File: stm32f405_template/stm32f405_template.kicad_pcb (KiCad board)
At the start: 2 copper layers, 51 x 71 mm, 55 parts, among them J1 USB_B, J2 Conn_01x08, J3 Conn_01x08, J4 Conn_01x02, J5 Conn_01x08, J6 Conn_01x08, J7 Conn_01x02, J8 Conn_01x02, Q1 2N3904, Q2 2N3904, SW1 SW_RESET, U1 STM32F405RGTx, U2 MCP1700-3302E_TO92, Y1 14MHz, Y2 32.768 kHz

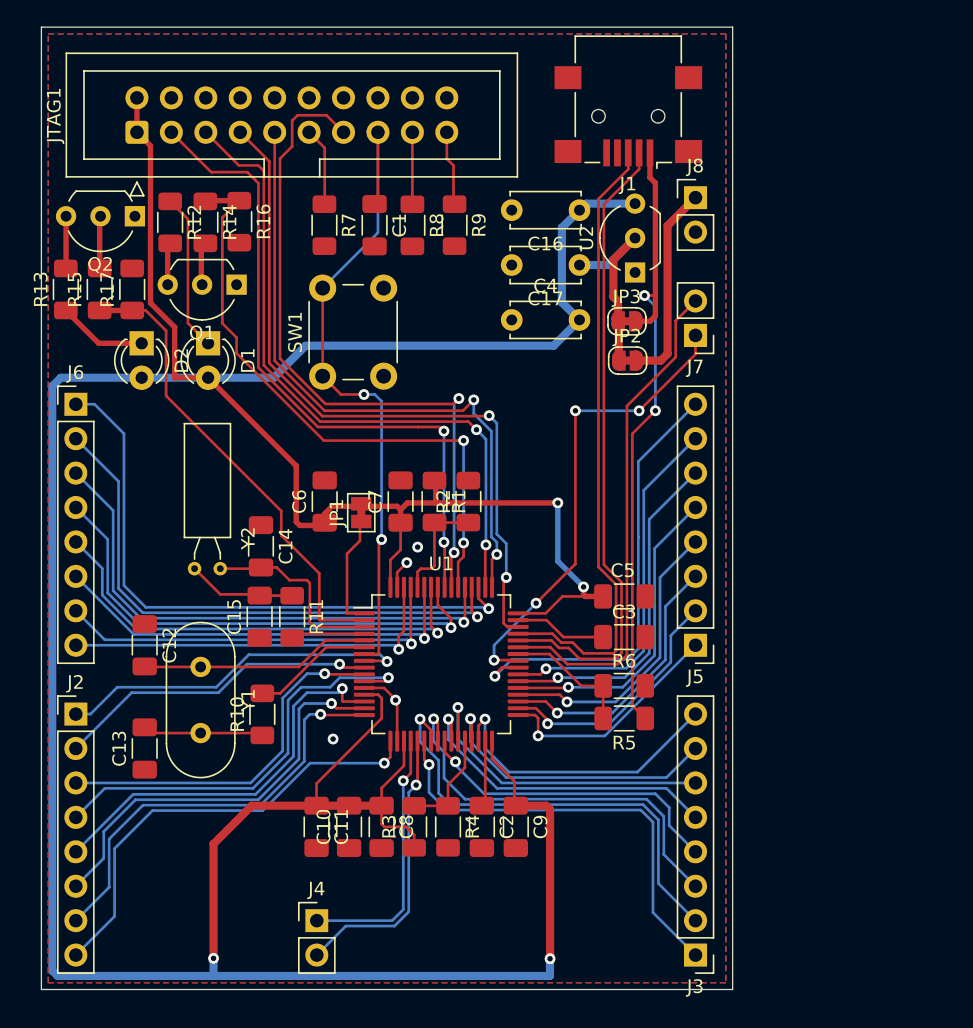
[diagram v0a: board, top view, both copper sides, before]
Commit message: Geographic re-annotate and cleanup
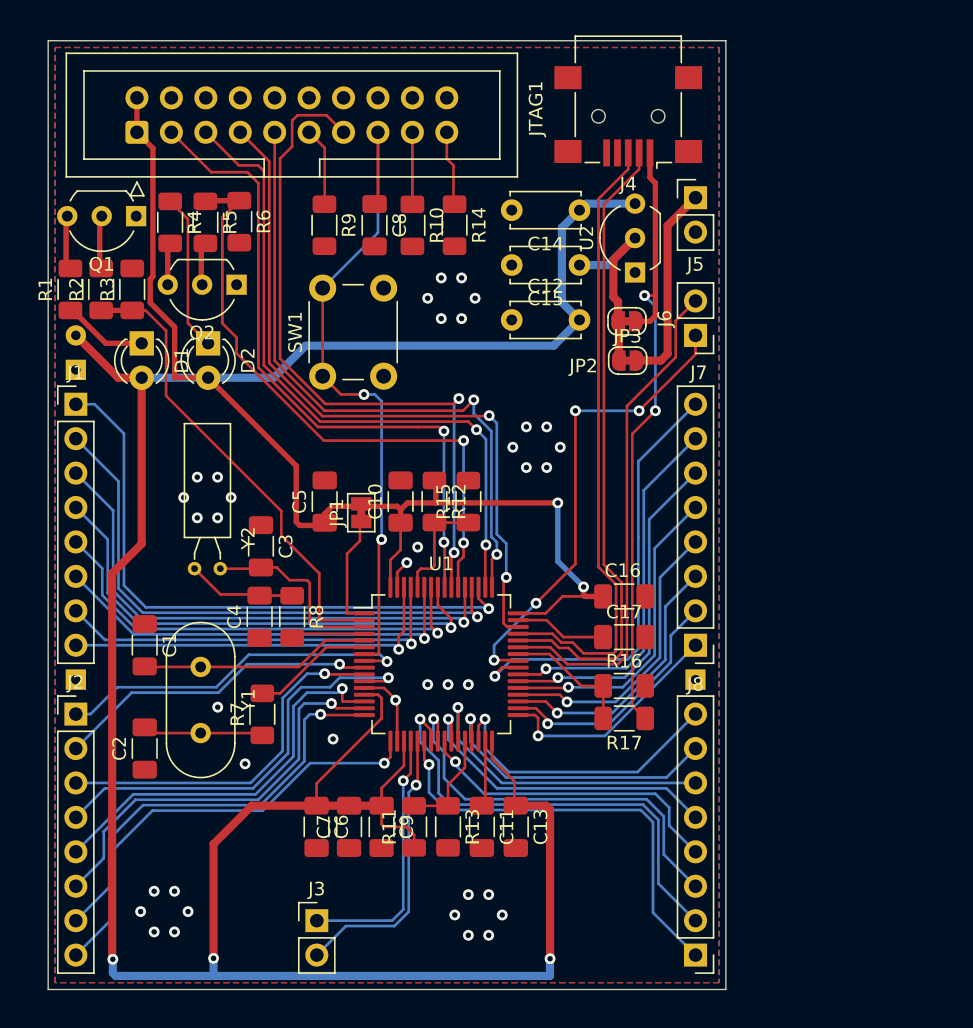
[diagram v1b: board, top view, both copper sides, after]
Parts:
- added TP100: TestPoint, TestPoint:TestPoint_THTPad_1.5x1.5mm_Drill0.7mm, B.Cu at (197.8, 97.6)
- added TP101: TestPoint, TestPoint:TestPoint_THTPad_D1.5mm_Drill0.7mm, B.Cu at (152.0, 72.2)
- added TP102: TestPoint, TestPoint:TestPoint_THTPad_1.5x1.5mm_Drill0.7mm, B.Cu at (152.0, 74.8)
- added TP103: TestPoint, TestPoint:TestPoint_THTPad_1.5x1.5mm_Drill0.7mm, B.Cu at (152.0, 97.6)
- moved R1 0.34 mm to (151.6, 68.8)
- moved R2 0.11 mm to (153.9, 68.8)
- moved Q1 0.09 mm to (156.5, 63.4)
- renumbered C12 to C1, C7 to C10, C2 to C11, C4 to C12, C9 to C13, C16 to C14, C17 to C15, C5 to C16, C3 to C17, C13 to C2, C14 to C3, C15 to C4, C6 to C5, C11 to C6, C10 to C7, C1 to C8, C8 to C9, D2 to D1, D1 to D2, J6 to J1, J4 to J3, J1 to J4, J8 to J5, J7 to J6, J5 to J7, J3 to J8, JP3 to JP2, JP2 to JP3, Q2 to Q1, Q1 to Q2, R13 to R1, R8 to R10, R3 to R11, R1 to R12, R4 to R13, R9 to R14, R2 to R15, R6 to R16, R5 to R17, R15 to R2, R17 to R3, R12 to R4, R14 to R5, R16 to R6, R10 to R7, R11 to R8, R7 to R9
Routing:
- net +3.3V: track 281.9 -> 278.5 mm, vias 4 -> 5
- net GND: vias 4 -> 39
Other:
- board size 51 x 71 mm -> 50 x 70 mm

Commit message: Silkscreen cleanup
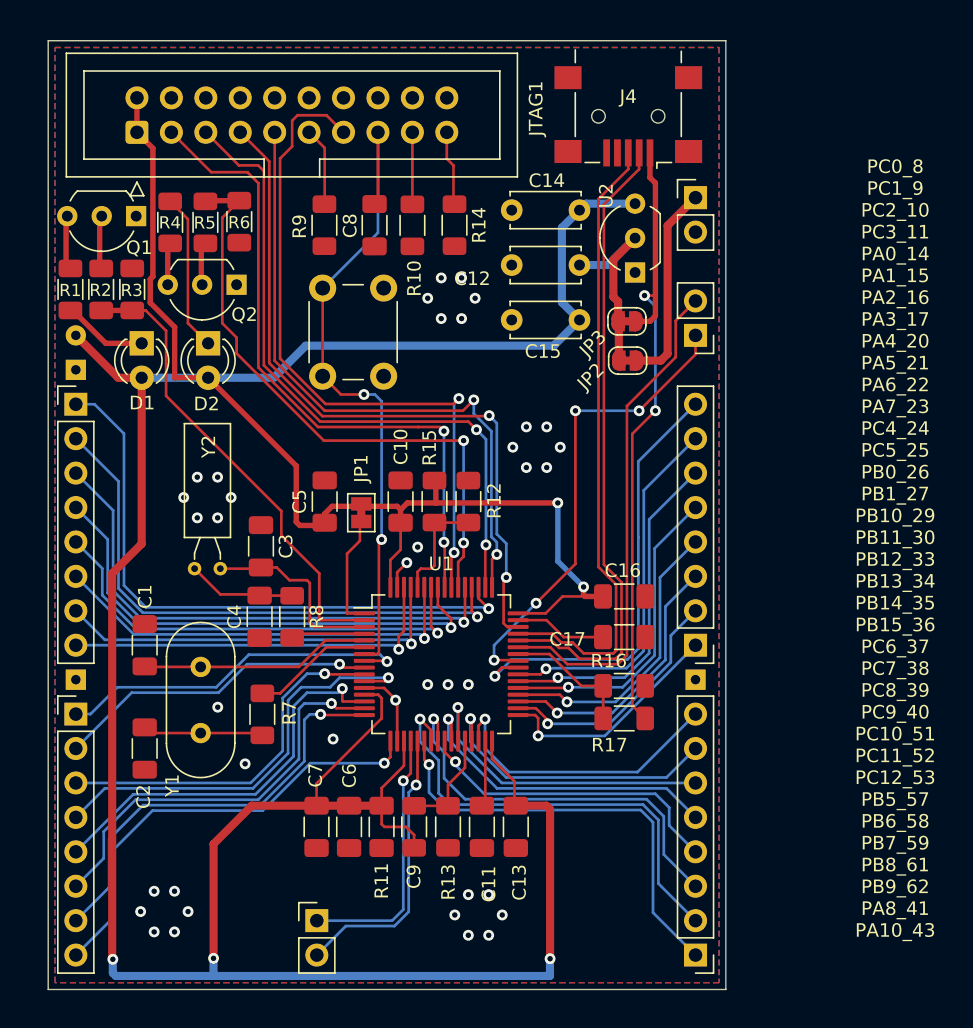
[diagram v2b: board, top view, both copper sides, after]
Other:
- board text added: "Breadboard Guides"
- board text added: "PC0_8 PC1_9 PC2_10 PC3_11 PA0_14 PA1_15 PA2_16 PA3_17 PA4_20 PA5_21 PA6_22 PA7_23 PC4_24 PC5_25 PB0_26 PB1_27 PB10_29 PB11_30 PB12_33 PB13_34 PB14_35 PB15_36 PC6_37 PC7_38 PC8_39 PC9_40 PC10_51 PC11_52 PC12_53 PB5_57 PB6_58 PB7_59 PB8_61 PB9_62 PA8_41 PA10_43"

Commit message: Tidied silkscreen and some routing cleanup
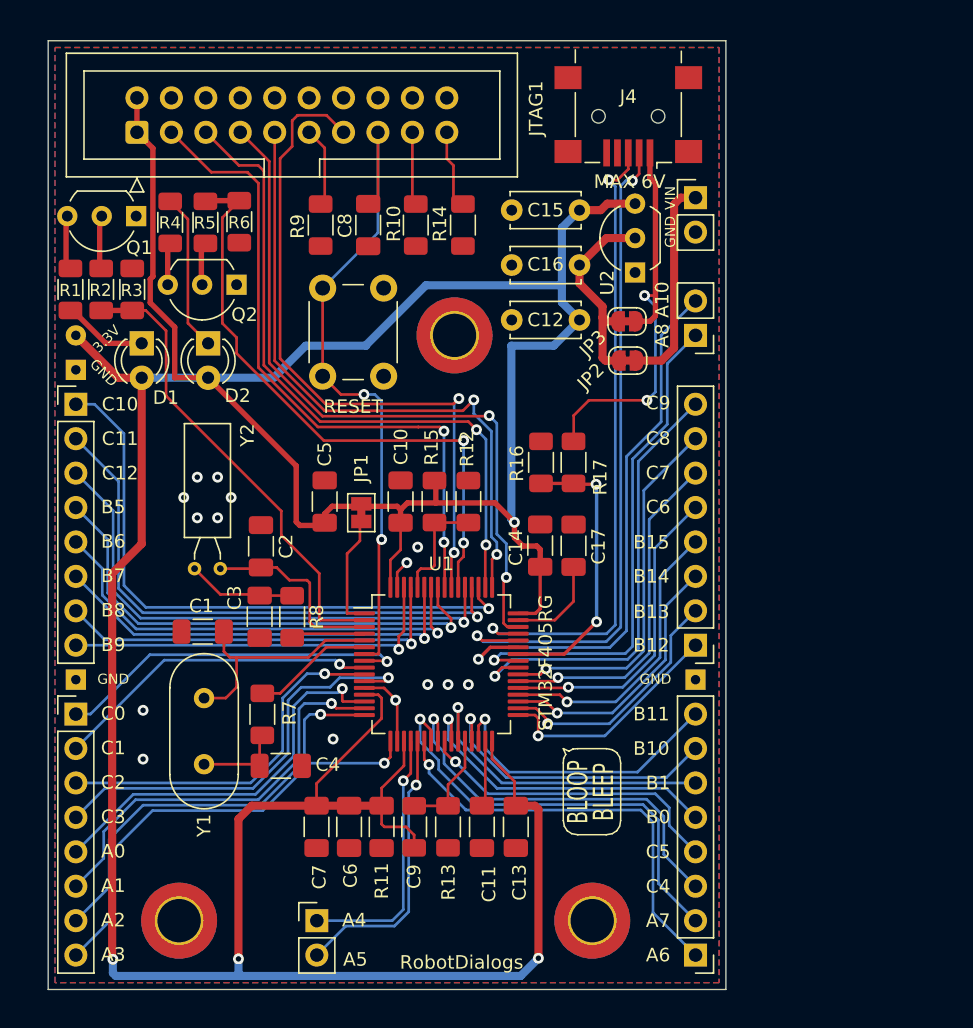
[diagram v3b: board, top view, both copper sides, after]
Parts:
- added H1: MountingHole_Pad, MountingHole:MountingHole_3.2mm_M3_DIN965_Pad_TopBottom, F.Cu at (159.7, 115.4)
- added H2: MountingHole_Pad, MountingHole:MountingHole_3.2mm_M3_DIN965_Pad_TopBottom, F.Cu at (180.0, 72.2)
- added H3: MountingHole_Pad, MountingHole:MountingHole_3.2mm_M3_DIN965_Pad_TopBottom, F.Cu at (190.1, 115.4)
- added LOGO1: logo1, My Stuff:Logo2, F.Cu at (175.0, 91.5)
- added LOGO101: Logo_Open_Hardware_Small, Symbol:OSHW-Symbol_6.7x6mm_SilkScreen, B.Cu at (175.0, 108.5)
- added LOGO2: logo1, My Stuff:Logo1, F.Cu at (190.1, 105.9)
- moved R17 19.3 mm to (188.8, 81.6), turned to -90 degrees
- moved R16 17.6 mm to (186.4, 81.6), turned to 90 degrees
- moved C4 10.1 mm to (167.2, 104.0), turned to 180 degrees
- moved C17 7.71 mm to (188.8, 87.8), turned to 90 degrees
- moved C14 7.25 mm to (186.3, 87.8), turned to 90 degrees
- moved C1 4.40 mm to (161.4, 94.1), turned to 0 degrees
- moved Y1 2.31 mm to (161.5, 99.0)
- moved R14 0.62 mm to (180.6, 64.1)
- moved C8 0.47 mm to (173.6, 64.1)
- moved R9 0.28 mm to (170.1, 64.1)
- moved R10 0.25 mm to (177.1, 64.1)
- renumbered C16 to C14, C14 to C15, C15 to C16, C3 to C2, C4 to C3, C2 to C4
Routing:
- net VBUS: track 47.2 -> 30.7 mm
- net /OTG_FS_VBUS: track 10.2 -> 21.0 mm, vias 0 -> 2
- net +3.3V: track 278.5 -> 285.2 mm, vias 5 -> 4
- net PA10_43: track 37.0 -> 41.5 mm, vias 0 -> 1
- net /OTG_FS_DM: track 46.9 -> 50.2 mm, vias 0 -> 2
- net PA8_41: track 34.7 -> 37.3 mm, vias 4 -> 1
- net Net-(C4-Pad2): track 8.94 -> 6.48 mm
- net /OTG_FS_DP: track 46.1 -> 47.6 mm, vias 0 -> 2
- net PA7_23: track 33.6 -> 32.6 mm
- net PA6_22: track 32.5 -> 31.6 mm
- net Net-(J5-Pad1): track 14.9 -> 15.6 mm
- net PC4_24: track 30.0 -> 29.3 mm
- net GND: vias 39 -> 15
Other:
- board text added: "3.3V"
- board text added: "70x50mm"
- board text added: "A0"
- board text added: "A1"
- board text added: "A10"
- board text added: "A2"
- board text added: "A3"
- board text added: "A4"
- board text added: "A5"
- board text added: "A6"
- board text added: "A7"
- board text added: "A8"
- board text added: "B0"
- board text added: "B1"
- board text added: "B10"
- board text added: "B11"
- board text added: "B12"
- board text added: "B13"
- board text added: "B14"
- board text added: "B15"
- board text added: "B5"
- board text added: "B6"
- board text added: "B7"
- board text added: "B8"
- board text added: "B9"
- board text added: "C0"
- board text added: "C1"
- board text added: "C10"
- board text added: "C11"
- board text added: "C12"
- board text added: "C2"
- board text added: "C3"
- board text added: "C4"
- board text added: "C5"
- board text added: "C6"
- board text added: "C7"
- board text added: "C8"
- board text added: "C9"
- board text added: "GND"
- board text added: "MAX 6V"
- board text added: "RESET"
- board text added: "RobotDialogs"
- board text added: "STM32F405 Breakout"
- board text added: "STM32F405RG"
- board text added: "VIN"
- board text added: "v1.0 Oct 2022"
- board text removed: "PC0_8 PC1_9 PC2_10 PC3_11 PA0_14 PA1_15 PA2_16 PA3_17 PA4_20 PA5_21 PA6_22 PA7_23 PC4_24 PC5_25 PB0_26 PB1_27 PB10_29 PB11_30 PB12_33 PB13_34 PB14_35 PB15_36 PC6_37 PC7_38 PC8_39 PC9_40 PC10_51 PC11_52 PC12_53 PB5_57 PB6_58 PB7_59 PB8_61 PB9_62 PA8_41 PA10_43"

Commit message: v1 schematic pdf with some assembly updates and notes
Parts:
- C1, C4: value 15pF -> 10pF
- C2, C3: value 9pF -> 15pF
- LOGO1: footprint My Stuff:Logo2 -> Symbol:OSHW-Symbol_6.7x6mm_SilkScreen; moved to B.Cu
- R7: value 100 -> 40max
- Y1: value 14MHz -> 16MHz
- turned LOGO1 to 180 degrees
